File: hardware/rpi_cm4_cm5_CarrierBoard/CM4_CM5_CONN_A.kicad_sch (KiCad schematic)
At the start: 69 parts, among them J19 RPI_CMx_A, J6 M20-9990245, J7 2998TR, Q12 2N7002, U19 SN74LVC1G125DBVR, U20 SN74LVC1G07DBVR, U21 MCP7940NT-I/MS, U5 SN74LVC1G125DBVR, Y2 32.768kHz

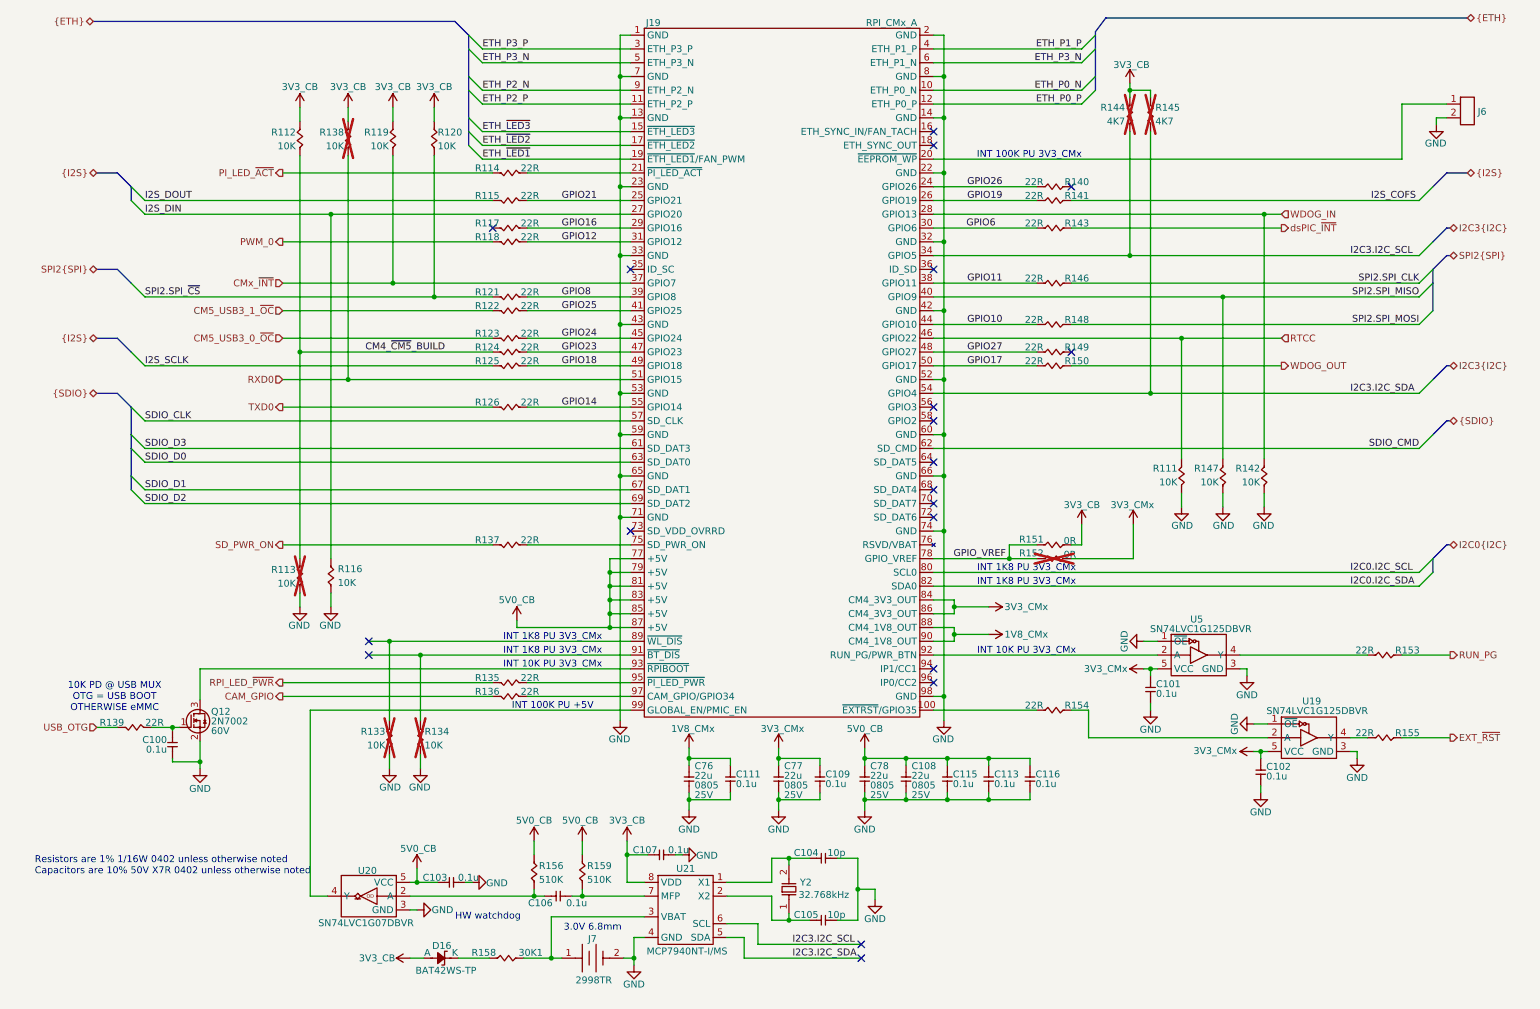
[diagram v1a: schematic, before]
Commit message: Significant update to schematics Add codec, Mikrobus, PIC32A Add power table, design notes for pinmux Add datasheets
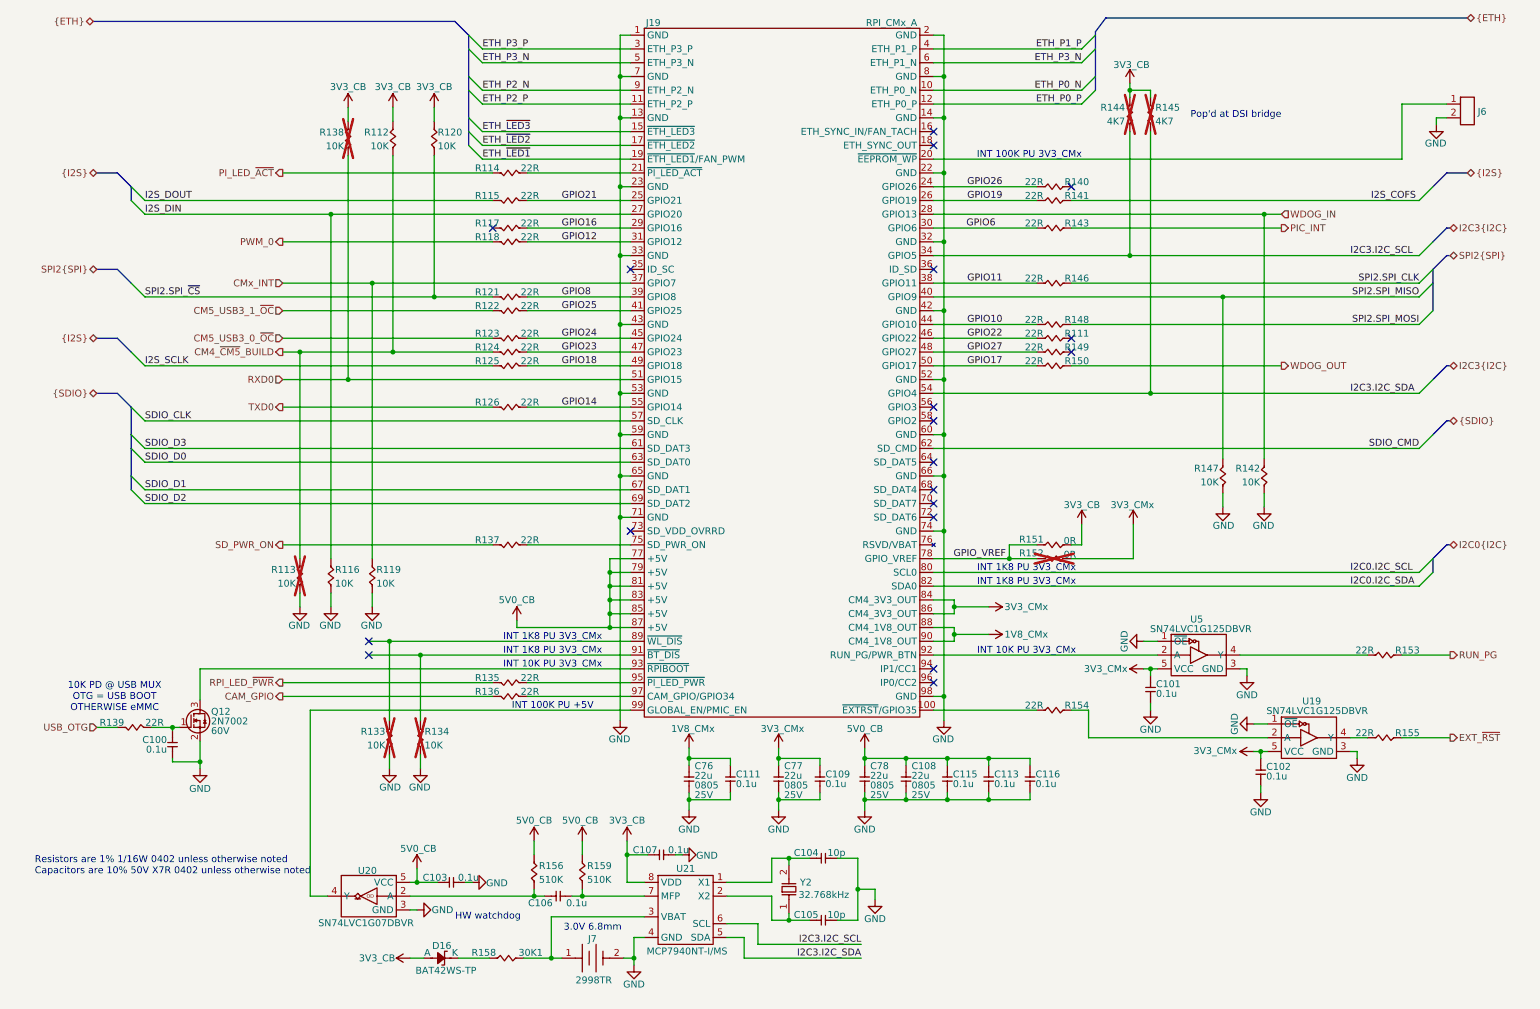
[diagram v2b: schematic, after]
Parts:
- removed R111: 10K, footprint:RES_0402, symbol KicadCompDb:Resistors/RES_SMT_00013
- added R111: 22R, footprint:RES_0402, symbol KicadCompDb:Resistors/RES_SMT_00015
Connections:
- net 3V3_CB: no longer R119.2
- net GND: now also R119.1
- net CMx_~{INT} renamed CMx_INT
- net CMx_INT: now also R119.2; no longer R119.1
- net RTCC renamed GPIO22
- net GPIO22: now also R111.1
- net dsPIC_~{INT} renamed PIC_INT
- no-connect marks 20 -> 19
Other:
- note added: "Pop'd at DSI bridge"
- moved on the sheet: R112, R119

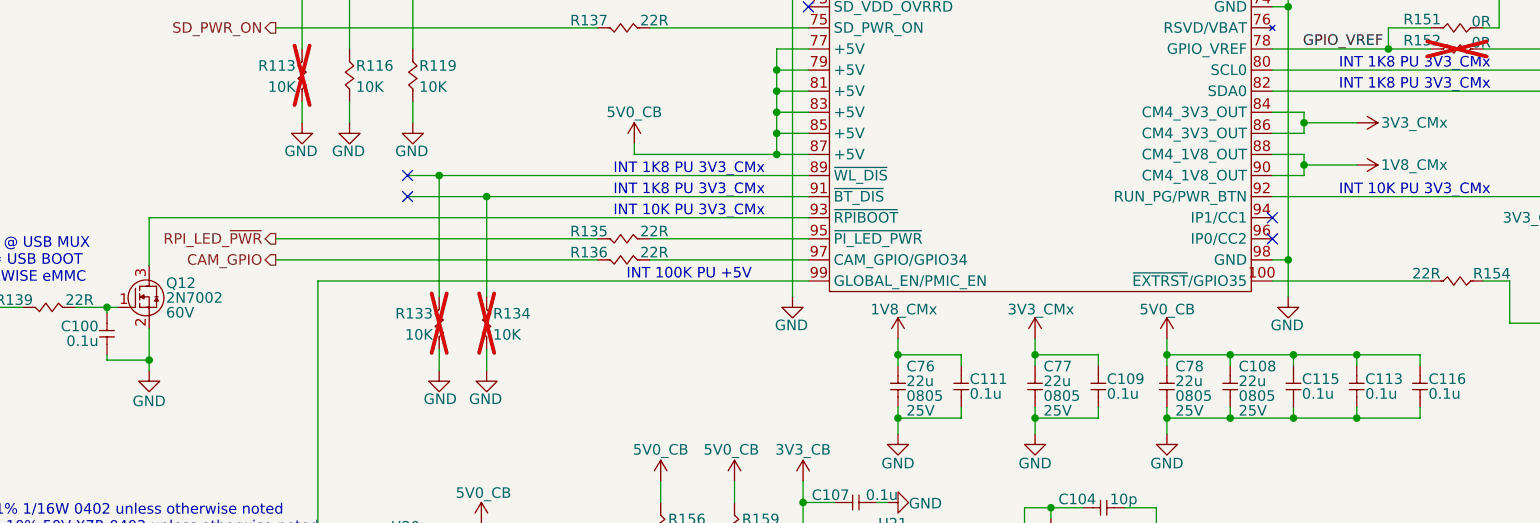
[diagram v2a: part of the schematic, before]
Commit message: Preliminary completion of RPI CMx schematics Cleaned up hierarchical root page
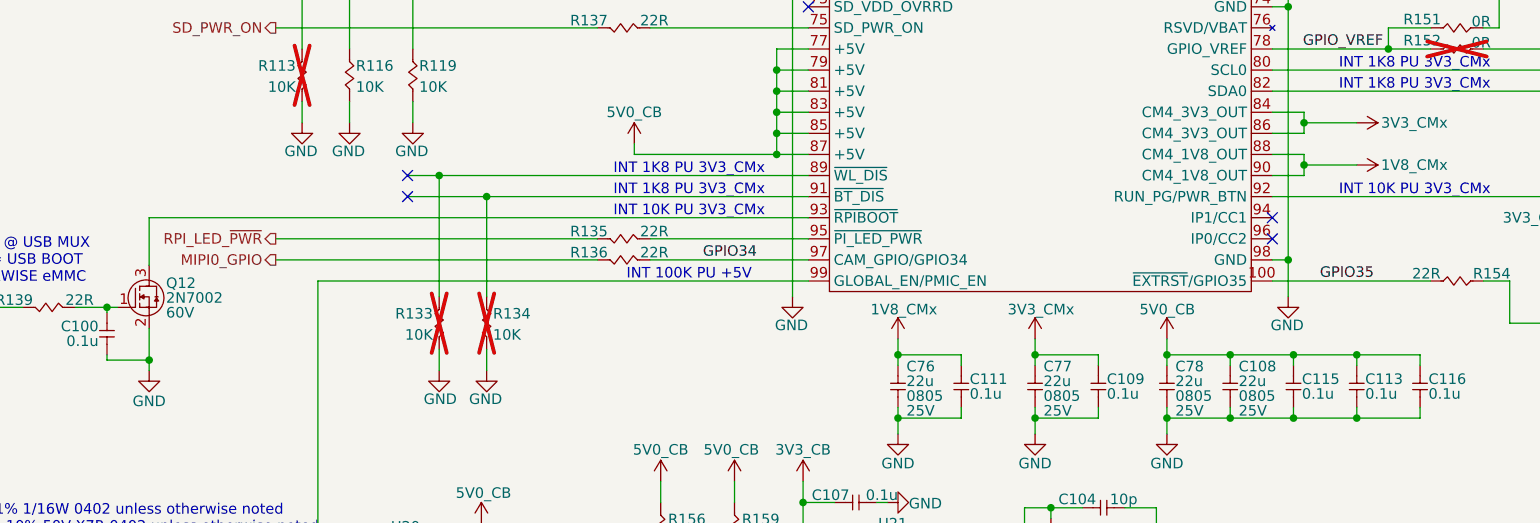
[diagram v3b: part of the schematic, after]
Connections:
- net GPIO35: now reaches J19.100 (~{EXTRST}/GPIO35), R154.1
- net GPIO34: now reaches J19.97 (CAM_GPIO/GPIO34), R136.1
- net CAM_GPIO renamed MIPI0_GPIO
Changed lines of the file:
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@@
+		)
+	)
+	(label "GPIO35"
+		(at 184.15 142.24 0)
+		(effects
+			(font
+				(size 1.27 1.27)
+			)
+			(justify left bottom)
 		)
 	)
@@
 		)
 	)
+	(label "GPIO34"
+		(at 109.855 139.7 0)
+		(effects
+			(font
+				(size 1.27 1.27)
+			)
+			(justify left bottom)
+		)
+	)
 	(label "I2C3.I2C_SCL"
 		(at 255.27 58.42 0)
@@
 		)
 	)
-	(hierarchical_label "CAM_GPIO"
+	(hierarchical_label "MIPI0_GPIO"
 		(shape output)
 		(at 58.42 139.7 180)

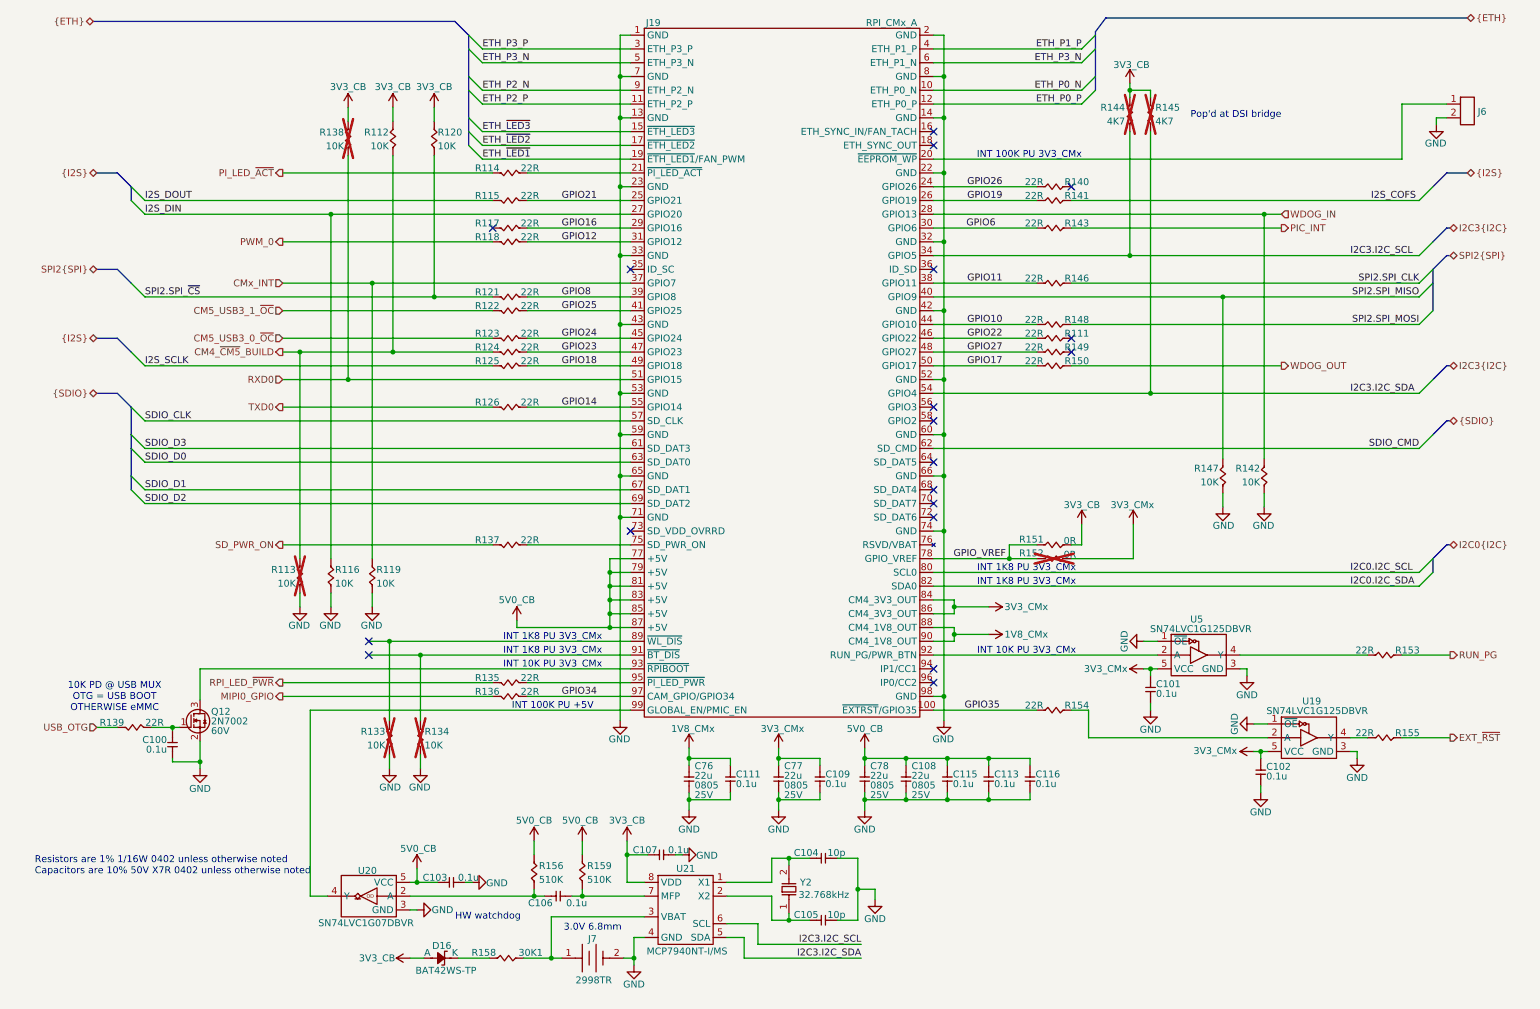
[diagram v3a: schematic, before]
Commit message: Add preliminary BOM and preliminary .pdf schmematics Add BOM option for I2C control of ILI2132A for CapTouch HMI Add BOM options and DNP / 0R resistors for CM4 - CM5 build options
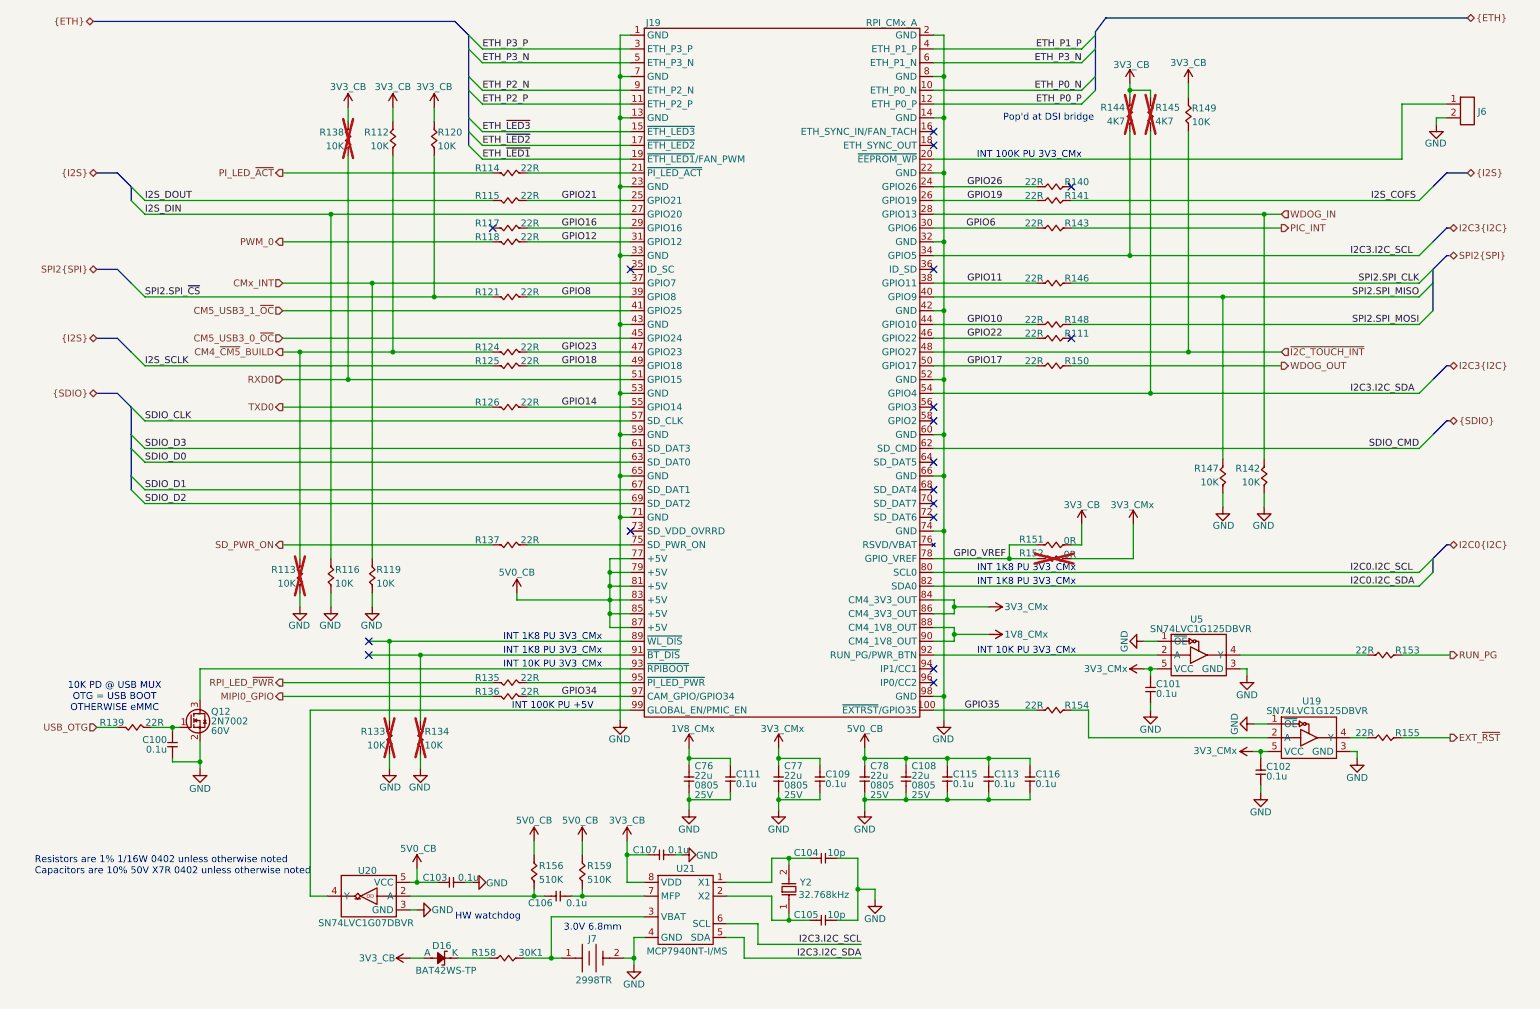
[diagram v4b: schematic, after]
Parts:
- removed R122, R123, R149: 22R, footprint:RES_0402, symbol KicadCompDb:Resistors/RES_SMT_00015
- added R149: 10K, footprint:RES_0402, symbol KicadCompDb:Resistors/RES_SMT_00013
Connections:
- net GPIO24 is gone; now on net CM5_USB3_0_~{OC}: J19.45 (GPIO24)
- net GPIO25 is gone; now on net CM5_USB3_1_~{OC}: J19.41 (GPIO25)
- net 3V3_CB: now also R149.2
- net GPIO27 renamed ~{I2C_TOUCH_INT}
- net ~{I2C_TOUCH_INT}: now also R149.1
- no-connect marks 19 -> 18

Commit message: Added power input protection & filter Added dedicated QWIIC connector on RPI CMx I2C6 bus Adjusted power table and PinMux Updated schematics accordingly
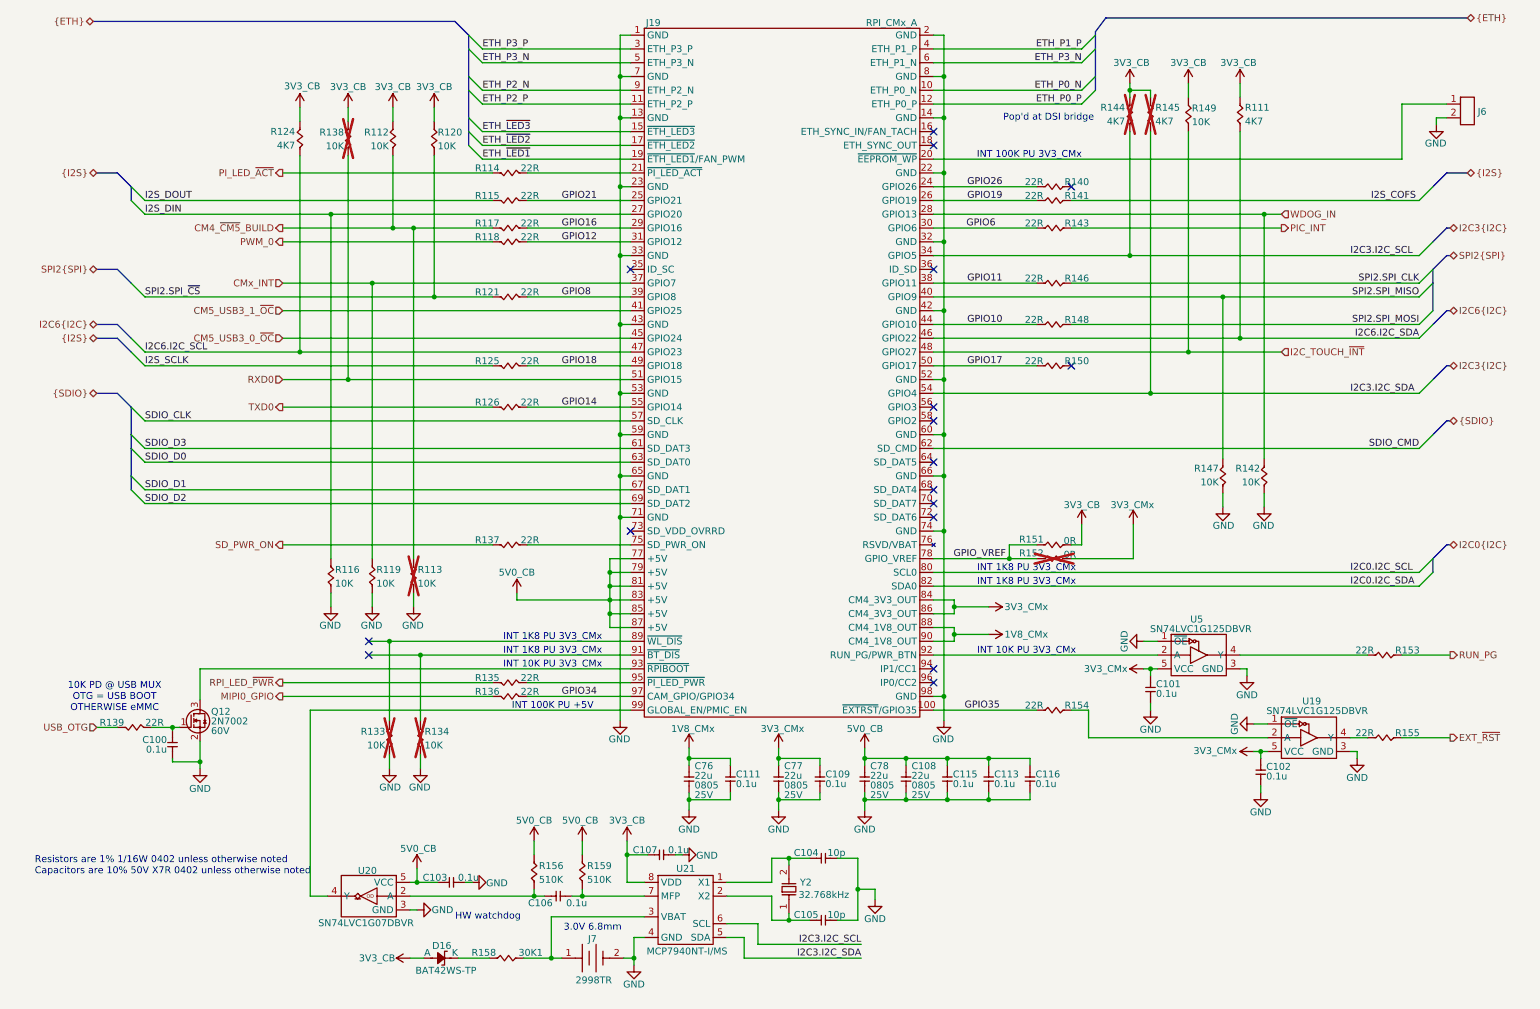
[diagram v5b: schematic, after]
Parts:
- removed R111, R124: 22R, footprint:RES_0402, symbol KicadCompDb:Resistors/RES_SMT_00015
- added R111, R124: 4K7, footprint:RES_0402, symbol KicadCompDb:Resistors/RES_SMT_00010
- J19: now in the parts list
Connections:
- net 3V3_CB: now also R111.2, R124.2
- net CM4_~{CM5}_BUILD: now also R117.2
- net GPIO22 renamed I2C6.I2C_SDA
- net I2C6.I2C_SDA: now also R111.1
- net GPIO23 renamed I2C6.I2C_SCL
- net I2C6.I2C_SCL: now also R124.1
- net WDOG_OUT: no longer names the net of R150.2
- net ~{I2C_TOUCH_INT} renamed I2C_TOUCH_~{INT}
- no-connect marks 18 -> 17
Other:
- moved on the sheet: R113
